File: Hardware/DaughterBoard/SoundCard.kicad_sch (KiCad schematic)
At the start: 19 parts, among them J5 AUDIO_OUT, U1 ATmega328P-PU, Y1 16MHz

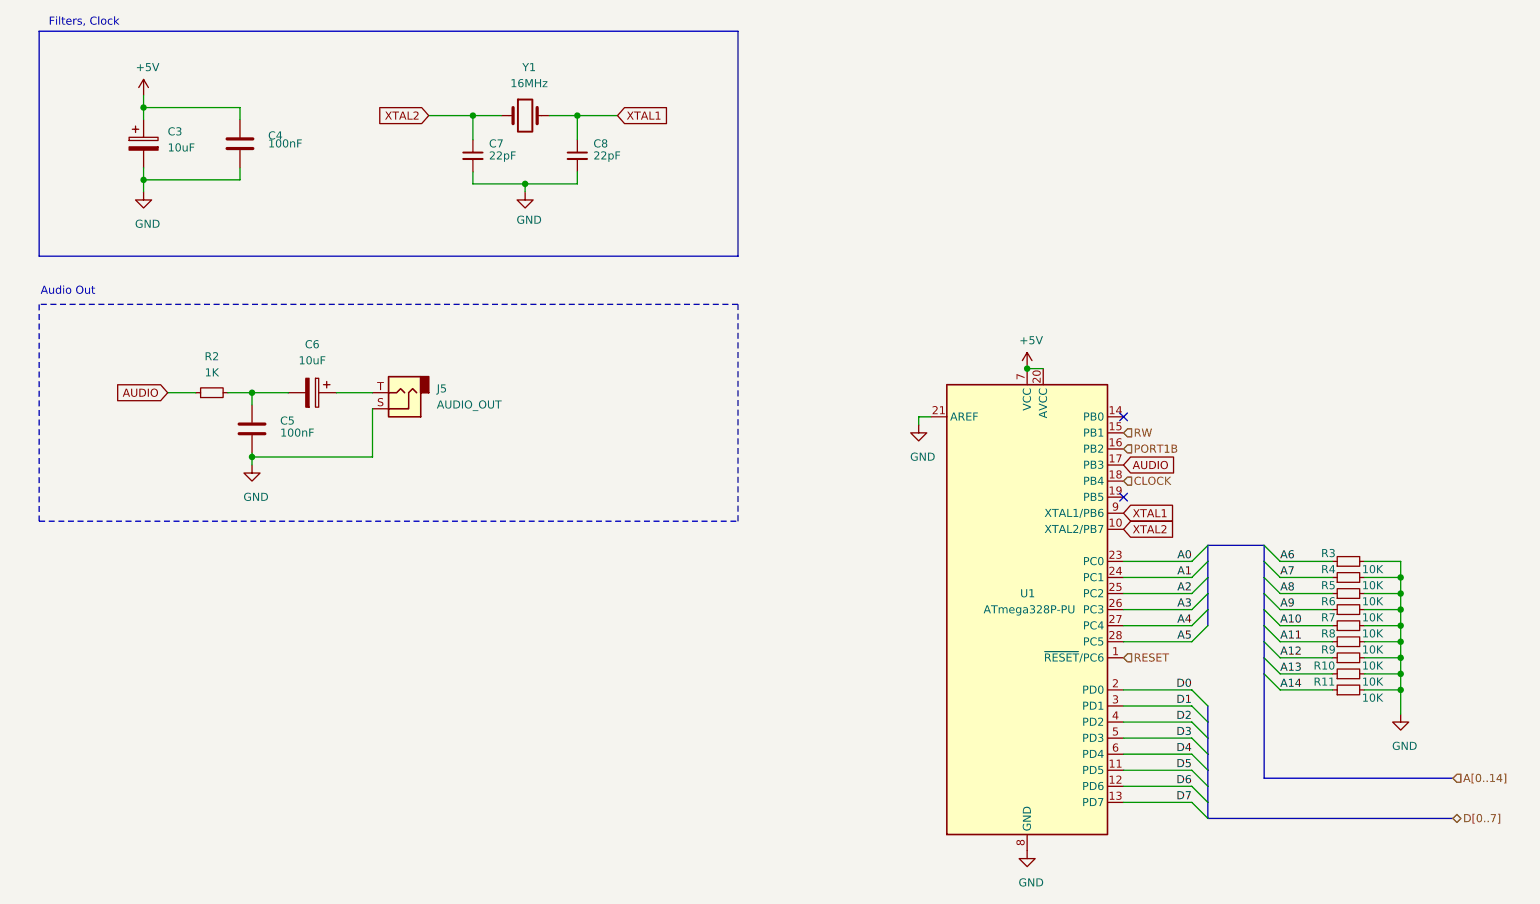
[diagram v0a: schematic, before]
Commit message: Implement APU and fix schematics
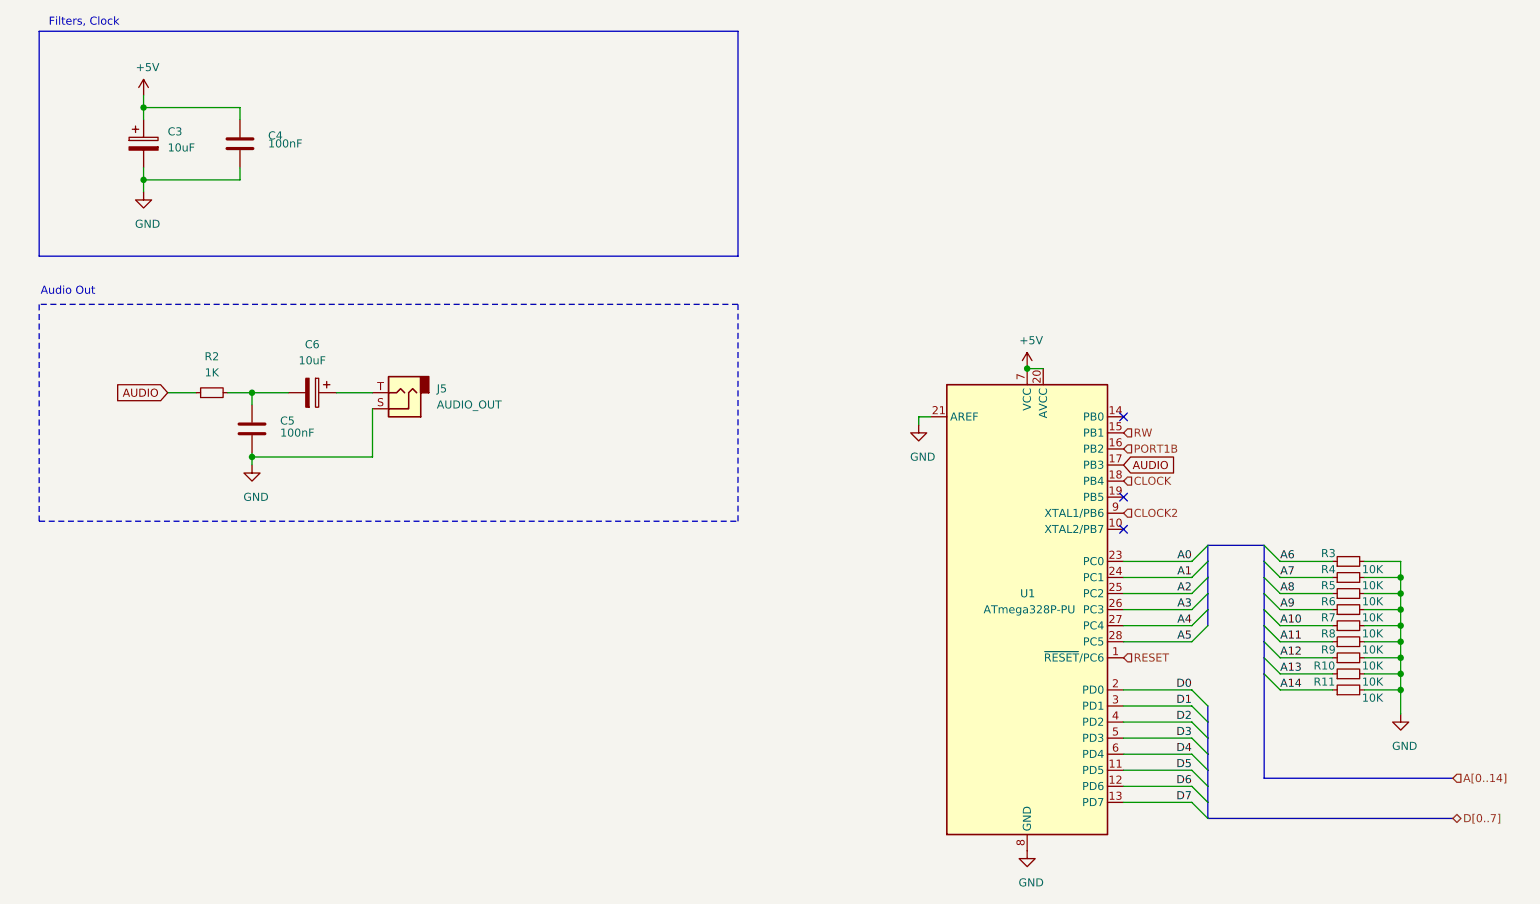
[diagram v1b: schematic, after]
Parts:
- removed C7, C8: 22pF, Capacitor_THT:C_Disc_D5.0mm_W2.5mm_P2.50mm, symbol Device:C_Small
- removed Y1: 16MHz, Crystal:Crystal_HC18-U_Vertical, symbol Device:Crystal
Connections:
- net XTAL1 renamed CLOCK2
- net XTAL2: no longer names the net of U1.10 (XTAL2/PB7)
- no-connect marks 2 -> 3
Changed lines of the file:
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@@
   (junction (at 50.165 74.295) (diameter 1.016) (color 0 0 0 0))
   (junction (at 50.165 84.455) (diameter 1.016) (color 0 0 0 0))
-  (junction (at 85.09 30.48) (diameter 1.016) (color 0 0 0 0))
-  (junction (at 93.345 41.275) (diameter 1.016) (color 0 0 0 0))
-  (junction (at 101.6 30.48) (diameter 1.016) (color 0 0 0 0))
   (junction (at 172.72 70.485) (diameter 1.016) (color 0 0 0 0))
   (junction (at 231.775 103.505) (diameter 1.016) (color 0 0 0 0))
@@
   (junction (at 231.775 121.285) (diameter 1.016) (color 0 0 0 0))
   (no_connect (at 187.96 90.805))
+  (no_connect (at 187.96 95.885))
   (no_connect (at 187.96 78.105))
   (bus_entry (at 198.755 100.965) (size 2.54 -2.54)
@@
     (stroke (width 0) (type solid) (color 0 0 0 0))
   )
-  (wire (pts (xy 78.105 30.48) (xy 85.09 30.48))
-    (stroke (width 0) (type solid) (color 0 0 0 0))
-  )
-  (wire (pts (xy 85.09 30.48) (xy 85.09 34.29))
-    (stroke (width 0) (type solid) (color 0 0 0 0))
-  )
-  (wire (pts (xy 85.09 30.48) (xy 89.535 30.48))
-    (stroke (width 0) (type solid) (color 0 0 0 0))
-  )
-  (wire (pts (xy 85.09 39.37) (xy 85.09 41.275))
-    (stroke (width 0) (type solid) (color 0 0 0 0))
-  )
-  (wire (pts (xy 85.09 41.275) (xy 93.345 41.275))
-    (stroke (width 0) (type solid) (color 0 0 0 0))
-  )
-  (wire (pts (xy 93.345 41.275) (xy 93.345 42.545))
-    (stroke (width 0) (type solid) (color 0 0 0 0))
-  )
-  (wire (pts (xy 93.345 41.275) (xy 101.6 41.275))
-    (stroke (width 0) (type solid) (color 0 0 0 0))
-  )
-  (wire (pts (xy 97.155 30.48) (xy 101.6 30.48))
-    (stroke (width 0) (type solid) (color 0 0 0 0))
-  )
-  (wire (pts (xy 101.6 30.48) (xy 101.6 34.29))
-    (stroke (width 0) (type solid) (color 0 0 0 0))
-  )
-  (wire (pts (xy 101.6 30.48) (xy 107.95 30.48))
-    (stroke (width 0) (type solid) (color 0 0 0 0))
-  )
-  (wire (pts (xy 101.6 41.275) (xy 101.6 39.37))
-    (stroke (width 0) (type solid) (color 0 0 0 0))
-  )
   (wire (pts (xy 155.575 78.105) (xy 155.575 79.375))
     (stroke (width 0) (type solid) (color 0 0 0 0))
@@
     (effects (font (size 1.27 1.27)) (justify right))
   )
-  (global_label "XTAL2" (shape input) (at 78.105 30.48 180)    (property "Intersheet References" "${INTERSHEET_REFS}" (id 0) (at 68.6646 30.5594 0)
-      (effects (font (size 1.27 1.27)) (justify right) hide)
-    )
-    (effects (font (size 1.27 1.27)) (justify right))
-  )
-  (global_label "XTAL1" (shape input) (at 107.95 30.48 0)    (property "Intersheet References" "${INTERSHEET_REFS}" (id 0) (at 117.3904 30.4006 0)
-      (effects (font (size 1.27 1.27)) (justify left) hide)
-    )
-    (effects (font (size 1.27 1.27)) (justify left))
-  )
   (global_label "AUDIO" (shape input) (at 187.96 85.725 0)    (property "Intersheet References" "${INTERSHEET_REFS}" (id 0) (at 197.5214 85.6456 0)
       (effects (font (size 1.27 1.27)) (justify left) hide)
@@
     (effects (font (size 1.27 1.27)) (justify left))
   )
-  (global_label "XTAL1" (shape input) (at 187.96 93.345 0)    (property "Intersheet References" "${INTERSHEET_REFS}" (id 0) (at 197.4004 93.2656 0)
-      (effects (font (size 1.27 1.27)) (justify left) hide)
-    )
-    (effects (font (size 1.27 1.27)) (justify left))
-  )
-  (global_label "XTAL2" (shape input) (at 187.96 95.885 0)    (property "Intersheet References" "${INTERSHEET_REFS}" (id 0) (at 197.4004 95.8056 0)
-      (effects (font (size 1.27 1.27)) (justify left) hide)
-    )
-    (effects (font (size 1.27 1.27)) (justify left))
-  )
   (hierarchical_label "RW" (shape input) (at 187.96 80.645 0)
     (effects (font (size 1.27 1.27)) (justify left))
@@
     (effects (font (size 1.27 1.27)) (justify left))
   )
+  (hierarchical_label "CLOCK2" (shape input) (at 187.96 93.345 0)
+    (effects (font (size 1.27 1.27)) (justify left))
+  )
   (hierarchical_label "RESET" (shape input) (at 187.96 116.205 0)
     (effects (font (size 1.27 1.27)) (justify left))
@@
     )
     (property "Datasheet" "" (id 3) (at 50.165 85.725 0)
-      (effects (font (size 1.27 1.27)) hide)
-    )
-  )
-  (symbol (lib_id "power:GND") (at 93.345 42.545 0) (unit 1)
-    (in_bom yes) (on_board yes)
-    (property "Reference" "#PWR0102" (id 0) (at 93.345 48.895 0)
-      (effects (font (size 1.27 1.27)) hide)
-    )
-    (property "Value" "GND" (id 1) (at 93.98 46.99 0))
-    (property "Footprint" "" (id 2) (at 93.345 42.545 0)
-      (effects (font (size 1.27 1.27)) hide)
-    )
-    (property "Datasheet" "" (id 3) (at 93.345 42.545 0)
       (effects (font (size 1.27 1.27)) hide)
     )
@@
     )
   )
-  (symbol (lib_id "Device:C_Small") (at 85.09 36.83 0) (unit 1)
-    (in_bom yes) (on_board yes)
-    (property "Reference" "C7" (id 0) (at 87.63 34.925 0)
-      (effects (font (size 1.27 1.27)) (justify left))
-    )
-    (property "Value" "22pF" (id 1) (at 87.63 36.83 0)
-      (effects (font (size 1.27 1.27)) (justify left))
-    )
-    (property "Footprint" "Capacitor_THT:C_Disc_D5.0mm_W2.5mm_P2.50mm" (id 2) (at 85.09 36.83 0)
-      (effects (font (size 1.27 1.27)) hide)
-    )
-    (property "Datasheet" "" (id 3) (at 85.09 36.83 0)
-      (effects (font (size 1.27 1.27)) hide)
-    )
-  )
-  (symbol (lib_id "Device:C_Small") (at 101.6 36.83 0) (unit 1)
-    (in_bom yes) (on_board yes)
-    (property "Reference" "C8" (id 0) (at 104.14 34.925 0)
-      (effects (font (size 1.27 1.27)) (justify left))
-    )
-    (property "Value" "22pF" (id 1) (at 104.14 36.83 0)
-      (effects (font (size 1.27 1.27)) (justify left))
-    )
-    (property "Footprint" "Capacitor_THT:C_Disc_D5.0mm_W2.5mm_P2.50mm" (id 2) (at 101.6 36.83 0)
-      (effects (font (size 1.27 1.27)) hide)
-    )
-    (property "Datasheet" "" (id 3) (at 101.6 36.83 0)
-      (effects (font (size 1.27 1.27)) hide)
-    )
-  )
   (symbol (lib_id "Device:CP") (at 33.02 34.925 0) (unit 1)
     (in_bom yes) (on_board yes)
@@
       (effects (font (size 1.27 1.27)) hide)
     )
-  )
-  (symbol (lib_id "Device:Crystal") (at 93.345 30.48 0) (unit 1)
-    (in_bom yes) (on_board yes)
-    (property "Reference" "Y1" (id 0) (at 93.98 22.86 0))
-    (property "Value" "16MHz" (id 1) (at 93.98 25.4 0))
-    (property "Footprint" "Crystal:Crystal_HC18-U_Vertical" (id 2) (at 93.345 30.48 0)
-      (effects (font (size 1.27 1.27)) hide)
-    )
-    (property "Datasheet" "" (id 3) (at 93.345 30.48 0)
-      (effects (font (size 1.27 1.27)) hide)
-    )

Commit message: Version 1.2
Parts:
- removed R10, R11, R3, R4, R5, R6, R7, R8, R9: 10K, Resistor_THT:R_Axial_DIN0207_L6.3mm_D2.5mm_P10.16mm_Horizontal, symbol Device:R_Small
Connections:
- net IRQ0B: now reaches U1.19 (PB5)
- no-connect marks 3 -> 2
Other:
- moved on the sheet: U1

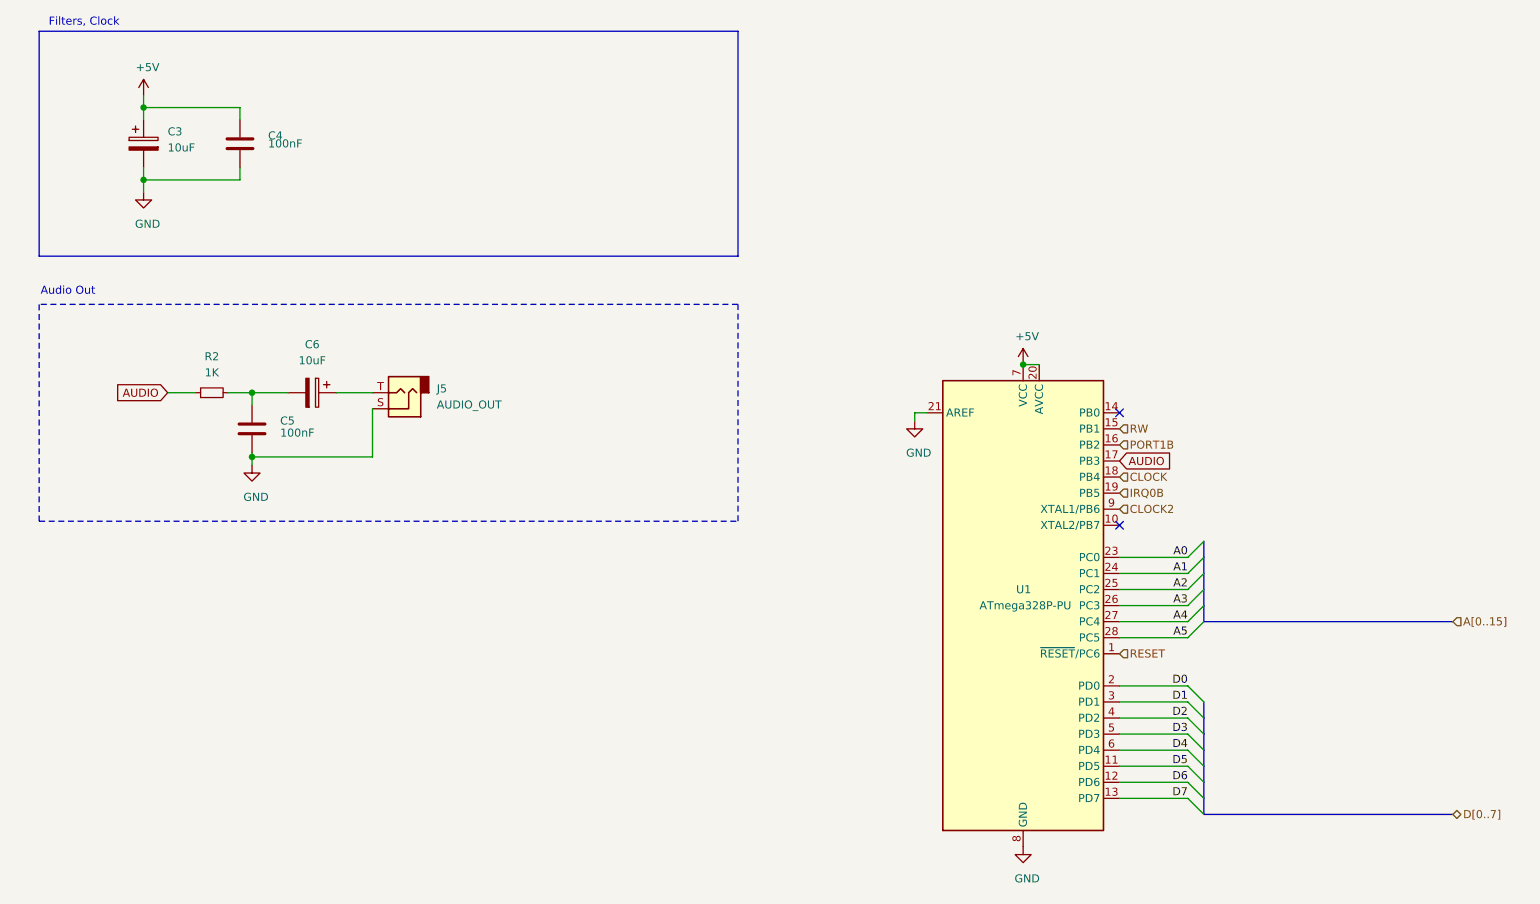
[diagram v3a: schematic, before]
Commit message: New PLD logic, VGA, DMA ...
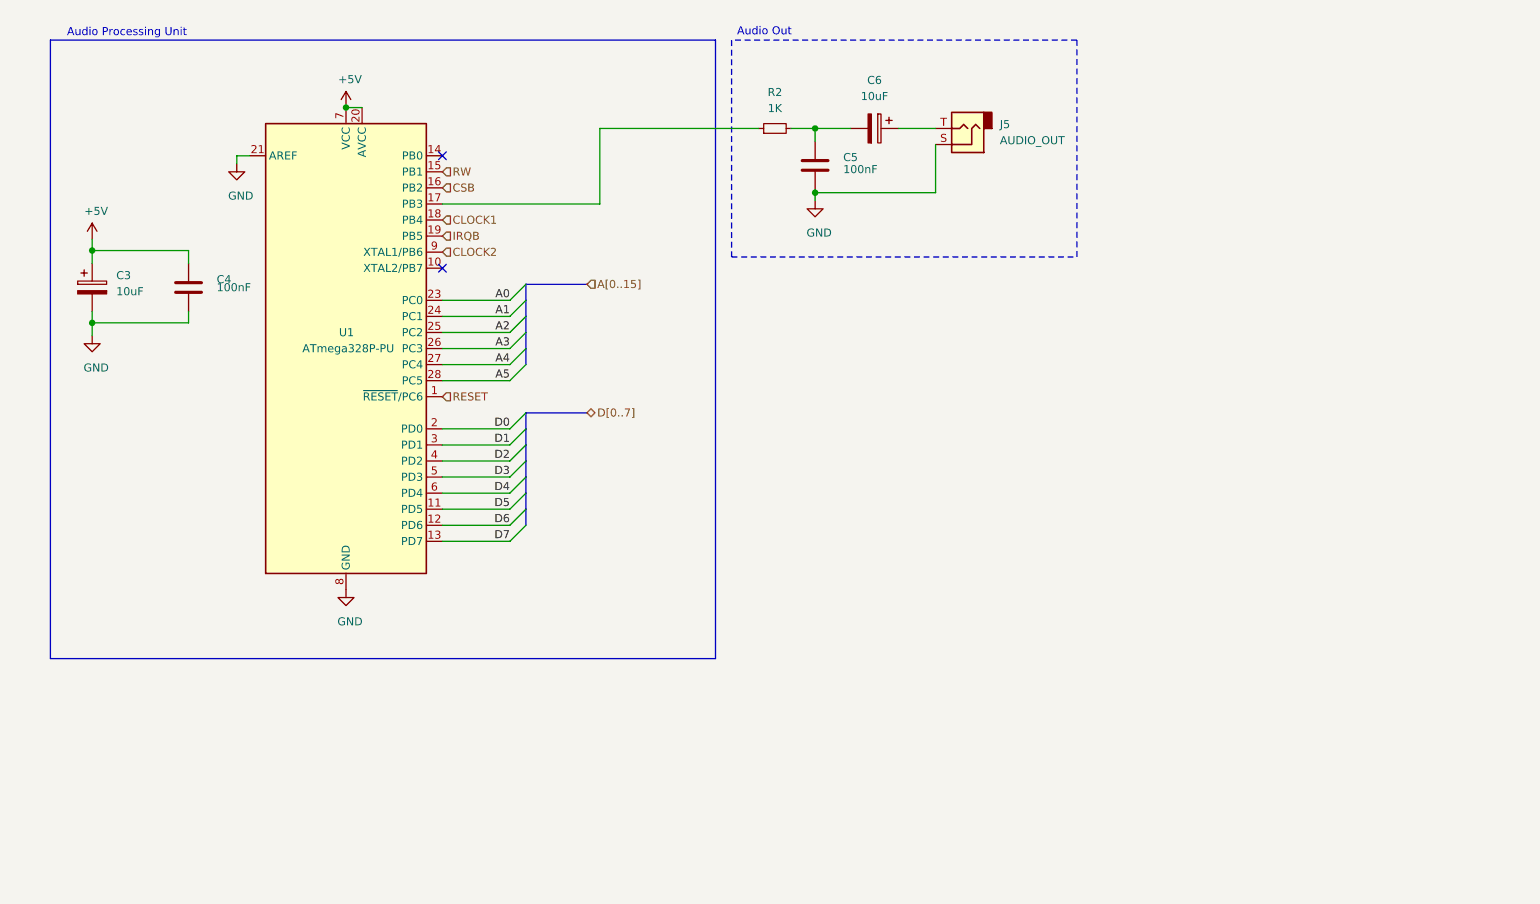
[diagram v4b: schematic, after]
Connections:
- net AUDIO: no longer names the net of R2.1, U1.17 (PB3)
- net CLOCK renamed CLOCK1
- net IRQ0B renamed IRQB
- net PORT1B renamed CSB
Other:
- note added: "Audio Processing Unit"
- note removed: "Filters, Clock"
- moved on the sheet: C3, C4, C5, C6, J5, R2, U1
